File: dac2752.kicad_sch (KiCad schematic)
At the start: 39 parts, among them U30 LTC2752B, U301 OPA2197D, U305 DG419D, U31 OPA2189DGK, U32 OPA2388DGK

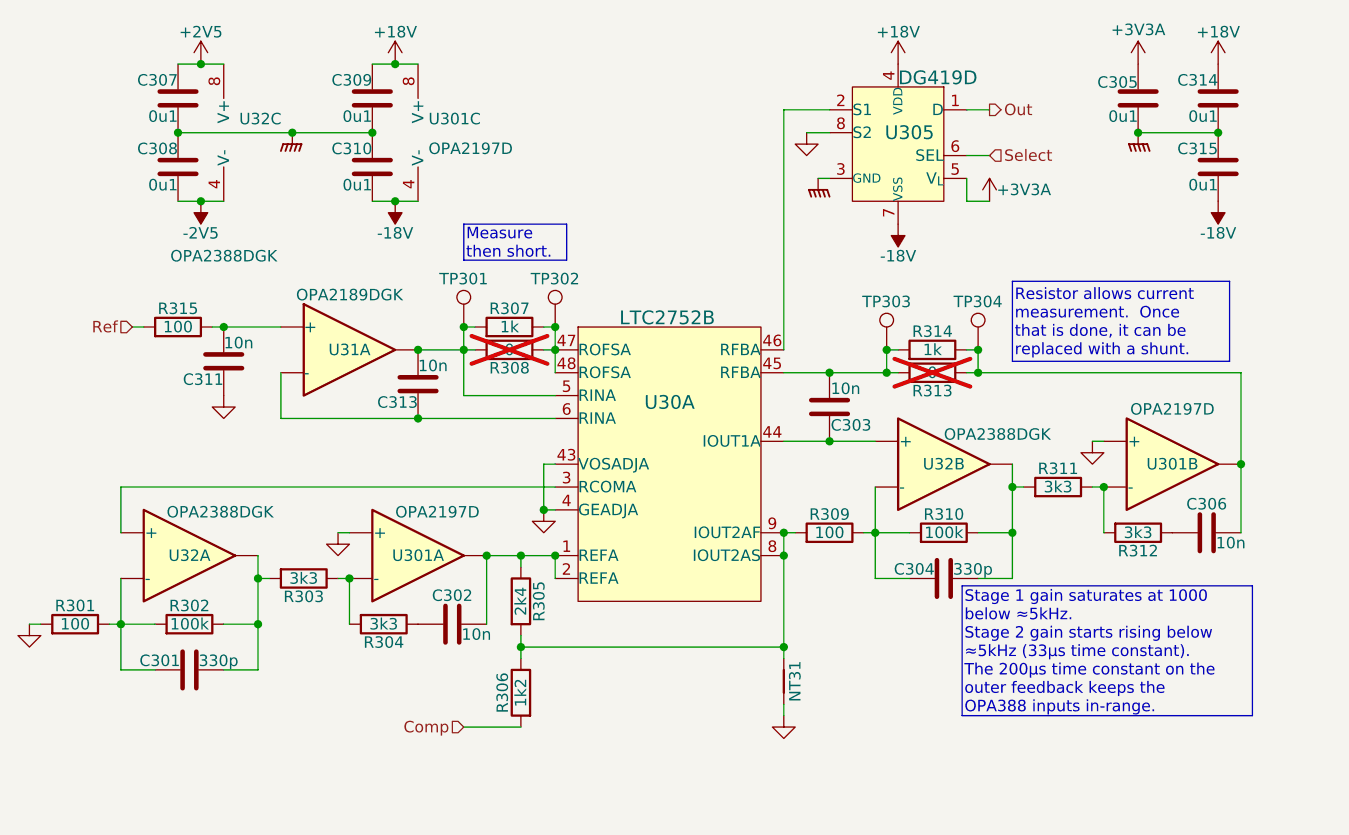
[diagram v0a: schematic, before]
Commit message: Whew.  DACs routed
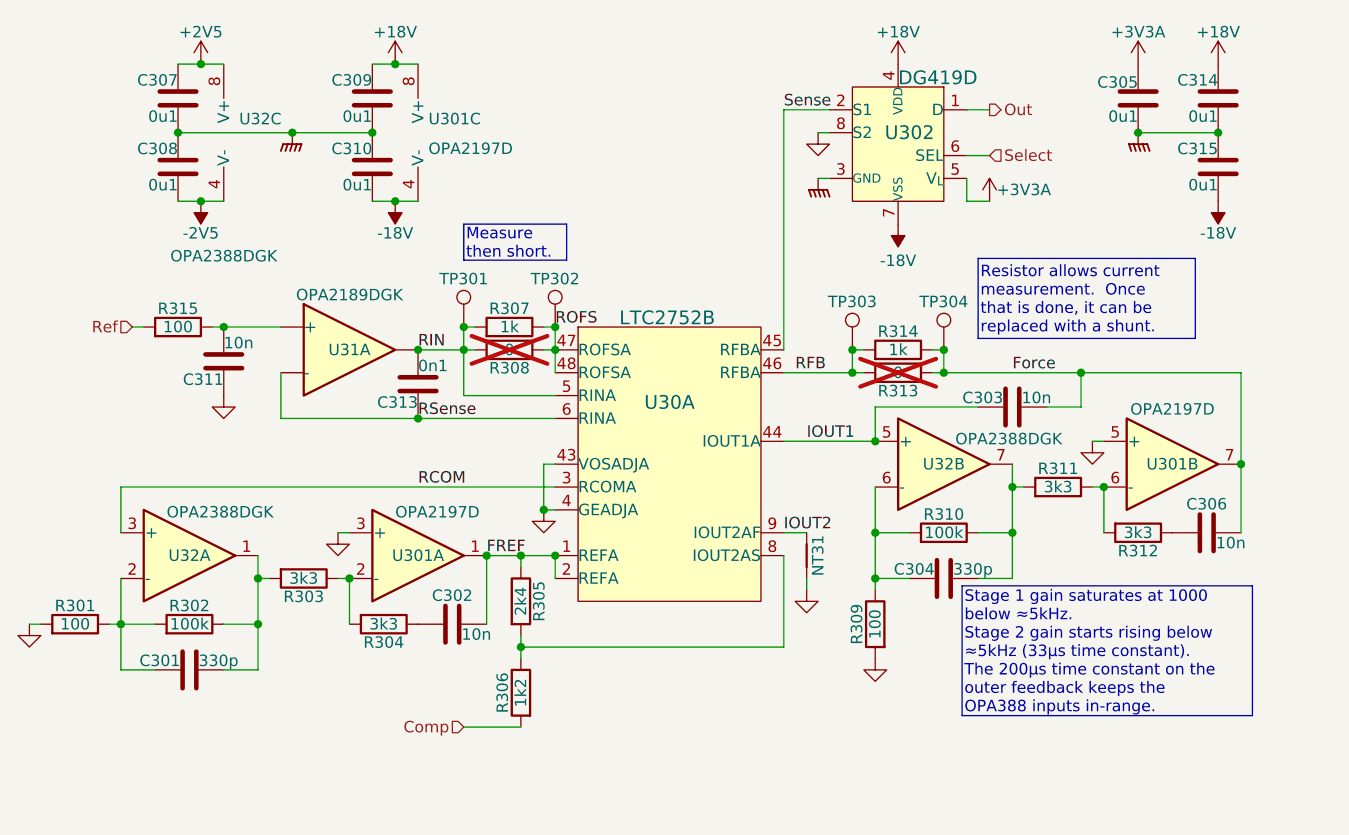
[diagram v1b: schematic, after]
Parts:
- C313: value 10n -> 0n1; footprint Capacitor_SMD:C_0603_1608Metric -> Capacitor_SMD:C_0402_1005Metric; LCSC C307500 -> C1546
- NT31: footprint NetTie:NetTie-2_SMD_Pad0.5mm -> Parts:NetTie-2_SMD_Pad0.5mm
- U30: footprint Package_QFP:LQFP-48_7x7mm_P0.5mm -> Parts:LQFP-48_7x7mm_P0.5mm
- U301: footprint Package_SO:SOIC-8_3.9x4.9mm_P1.27mm -> Parts:OPA2197; symbol Amplifier_Operational:OPA2197xD -> Parts:OPA2197D
- U31: footprint Package_SO:MSOP-8_3x3mm_P0.65mm -> Parts:OPA2189
- U32: footprint Package_SO:MSOP-8_3x3mm_P0.65mm -> Parts:OPA2388
- renumbered U305 to U302
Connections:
- net GND: now also R309.2
- net Force: now reaches C306.1, R313.1, R314.1, TP304.1, U301.7
- net Force: now also C303.2
- net IOUT1: now reaches U30.44 (IOUT1A), U32.5 (+)
- net IOUT1: now also C303.1; no longer C303.2
- net FREF: now reaches C302.1, R305.1, U30.1 (REFA), U30.2 (REFA), U301.1
- net RFB: now reaches R313.2, R314.2, TP303.1
- net RFB: now also U30.46 (RFBA); no longer C303.1, U30.45 (RFBA)
- net ROFS: now reaches R307.1, R308.1, TP302.1, U30.47 (ROFSA), U30.48 (ROFSA)
- net RIN: now reaches C313.1, R307.2, R308.2, TP301.1, U30.5 (RINA), U31.1
- net RCOM: now reaches U30.3 (RCOMA), U32.3 (+)
- net Sense: now reaches U302.2 (S1)
- net Sense: now also U30.45 (RFBA); no longer U30.46 (RFBA)
- net RSense: now reaches C313.2, U30.6 (RINA), U31.2 (-)
- net at R305.2, R306.1, U30.8 (IOUT2AS): no longer NT31.2, R309.2, U30.9 (IOUT2AF)
- new net IOUT2: NT31.2, U30.9 (IOUT2AF)
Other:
- moved on the sheet: C303, NT31, R309, R314, TP303, TP304

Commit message: Tweaks following spice simulation.
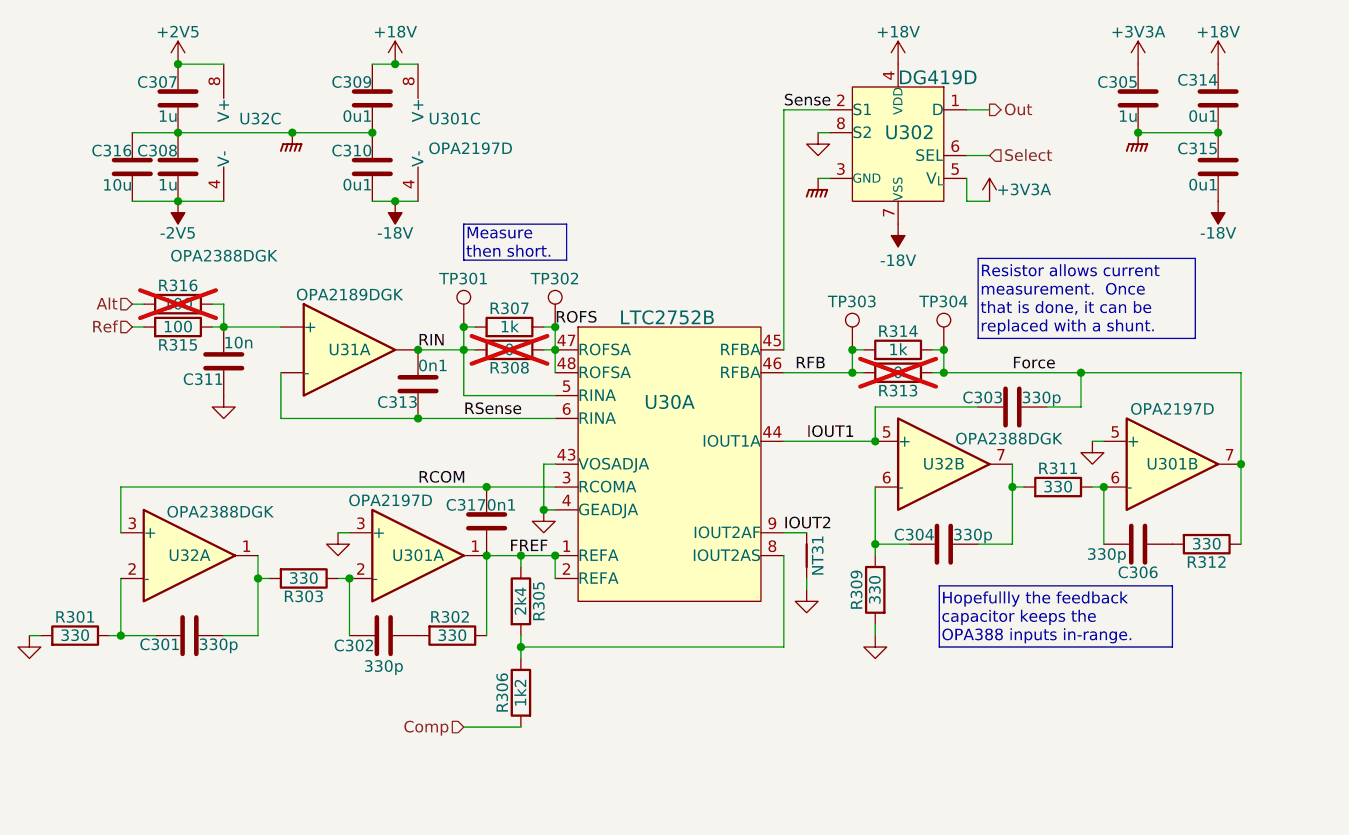
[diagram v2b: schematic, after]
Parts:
- removed R304: 3k3, Resistor_SMD:R_0603_1608Metric, symbol Device:R
- removed R310: 100k, Resistor_SMD:R_0603_1608Metric, symbol Device:R
- added C316: 10u, Capacitor_SMD:C_0603_1608Metric, symbol Device:C
- added C317: 0n1, Capacitor_SMD:C_0402_1005Metric, symbol Device:C
- added R316: 100, Resistor_SMD:R_0603_1608Metric, symbol Device:R
- C302, C303, C306: value 10n -> 330p; LCSC C307500 -> C1664
- C305, C307, C308: value 0u1 -> 1u; LCSC C307331 -> C52923
- R301, R309: value 100 -> 330; footprint Resistor_SMD:R_0603_1608Metric -> Resistor_SMD:R_0402_1005Metric; LCSC C23140 -> C25104
- R302: value 100k -> 330; footprint Resistor_SMD:R_0603_1608Metric -> Resistor_SMD:R_0402_1005Metric; LCSC C4216 -> C25104
- R303, R311, R312: value 3k3 -> 330; footprint Resistor_SMD:R_0603_1608Metric -> Resistor_SMD:R_0402_1005Metric; LCSC C22978 -> C25104
- R315: footprint Resistor_SMD:R_0402_1005Metric -> Resistor_SMD:R_0603_1608Metric
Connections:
- net -2V5: now also C316.2
- net FREF: now also R302.1, C317.2; no longer C302.1
- net Force: now also R312.1; no longer C306.1
- net GNDPWR: now also C316.1
- net RCOM: now also C317.1
- net at R311.1, U301.6 (-): now also C306.2; no longer R312.2
- net at R303.1, U301.2 (-): now also C302.2
- net at C301.1, R303.2, U32.1: no longer R302.1
- net at C301.2, R301.1, U32.2 (-): no longer R302.2
- net at C311.1, R315.1, U31.3 (+): now also R316.1
- new net: C302.1, R302.2
- new net: C306.1, R312.2
- new net Alt: R316.2
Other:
- moved on the sheet: C301, C302, C304, C306, R301, R309, R312

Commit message: About to delete scan...
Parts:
- R308, R313: Stock (none) -> 40
- R316: LCSC C25076 -> (none); Stock (none) -> 40
- TP301, TP302, TP303, TP304: Stock (none) -> -
- U301: Stock (none) -> 30
- U31: Stock (none) -> 15
- U32: Stock (none) -> 14

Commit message: Scan deleted.
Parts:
- R315: LCSC C25076 -> C22775
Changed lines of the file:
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@@
 			)
 		)
-		(property "Datasheet" "50V"
+		(property "Datasheet" "X7R, 50V"
 			(at 184.15 50.8 0)
 			(effects
@@
 			)
 		)
-		(property "Datasheet" "50V"
+		(property "Datasheet" "X7R, 50V"
 			(at 90.17 50.8 0)
 			(effects
@@
 			)
 		)
-		(property "LCSC" "C25076"
+		(property "LCSC" "C22775"
 			(at 68.58 76.2 90)
 			(effects
@@
 			)
 		)
-		(property "Datasheet" "50V"
+		(property "Datasheet" "X7R, 50V"
 			(at 90.17 58.42 0)
 			(effects
@@
 			)
 		)
-		(property "Datasheet" "50V"
+		(property "Datasheet" "X7R, 50V"
 			(at 184.15 58.42 0)
 			(effects

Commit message: Most blocks there....
About to restore scan.
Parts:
- removed C313: 0n1, Capacitor_SMD:C_0402_1005Metric, symbol Device:C
- removed C316: 10u, Capacitor_SMD:C_0603_1608Metric, symbol Device:C
- removed NT31: NetTie_2, Parts:NetTie-2_SMD_Pad0.5mm, symbol Parts:NetTie_2
- removed R305: 2k4, Resistor_SMD:R_0402_1005Metric, symbol Device:R
- removed R306: 1k2, Resistor_SMD:R_0402_1005Metric, symbol Device:R
- removed R307, R314: 1k, Resistor_SMD:R_0402_1005Metric, symbol Device:R
- removed R308, R313: 0, Resistor_SMD:R_0603_1608Metric, symbol Device:R
- removed TP301, TP302, TP303, TP304: TestPoint, Parts:TestPoint, symbol Connector:TestPoint
- added U34: OPA2388DGK, Parts:OPA2388, symbol Parts:OPA2388DGK
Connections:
- net RFB is gone; now on net Force: U30.46 (RFBA)
- net ROFS is gone; now on net RIN: U30.47 (ROFSA), U30.48 (ROFSA)
- net GND: now also R309.1, U34.5 (+); no longer R309.2
- net at C304.2, U32.6 (-): now also R309.2; no longer R309.1
- net at U30.8 (IOUT2AS): now also U34.6 (-)
- net IOUT2: no longer names the net of U30.9 (IOUT2AF)
- net IOUT2: now also U34.7
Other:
- moved on the sheet: C303, C304, C305, C306, C307, C308, C309, C310, C314, C315, R309, R311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

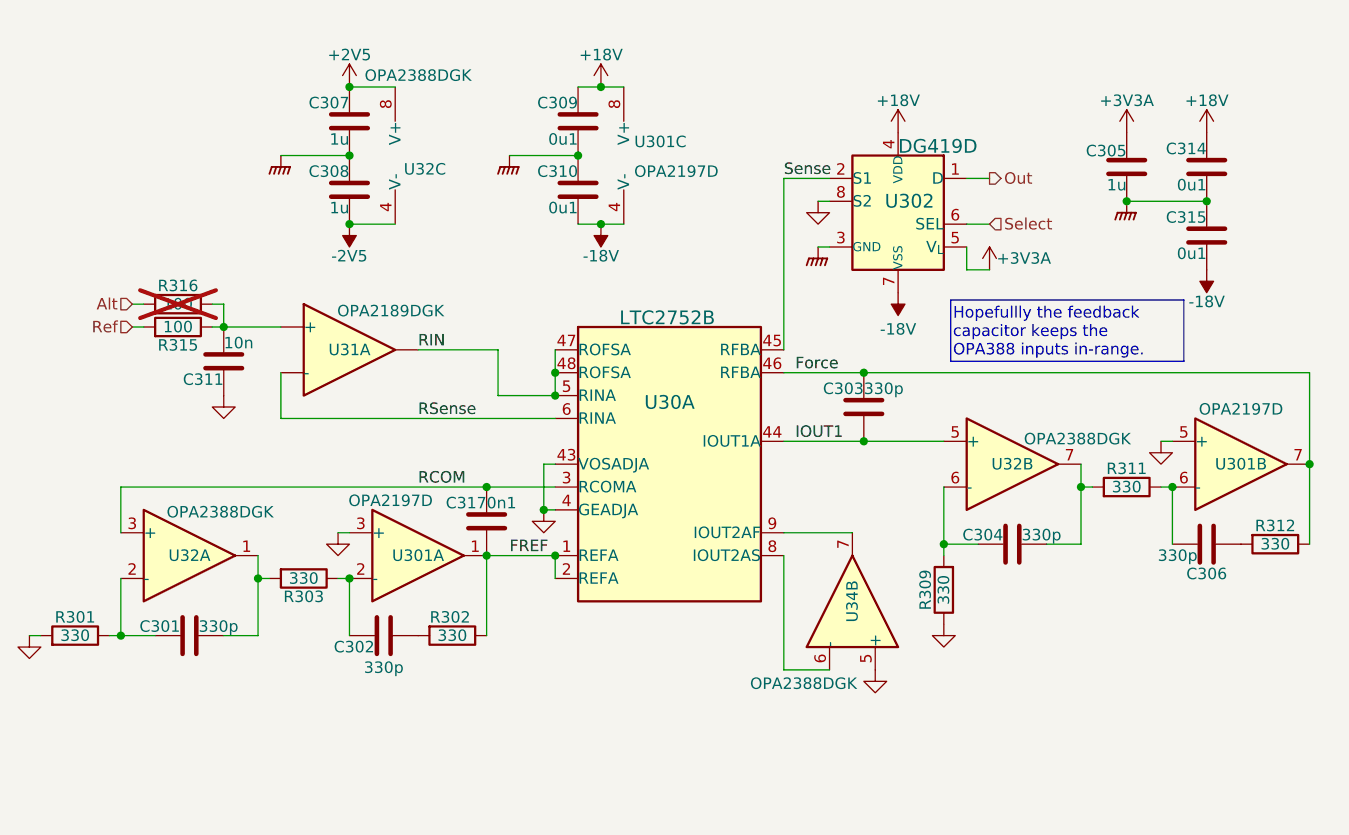
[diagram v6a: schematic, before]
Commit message: Put ref filtering into the schematic.
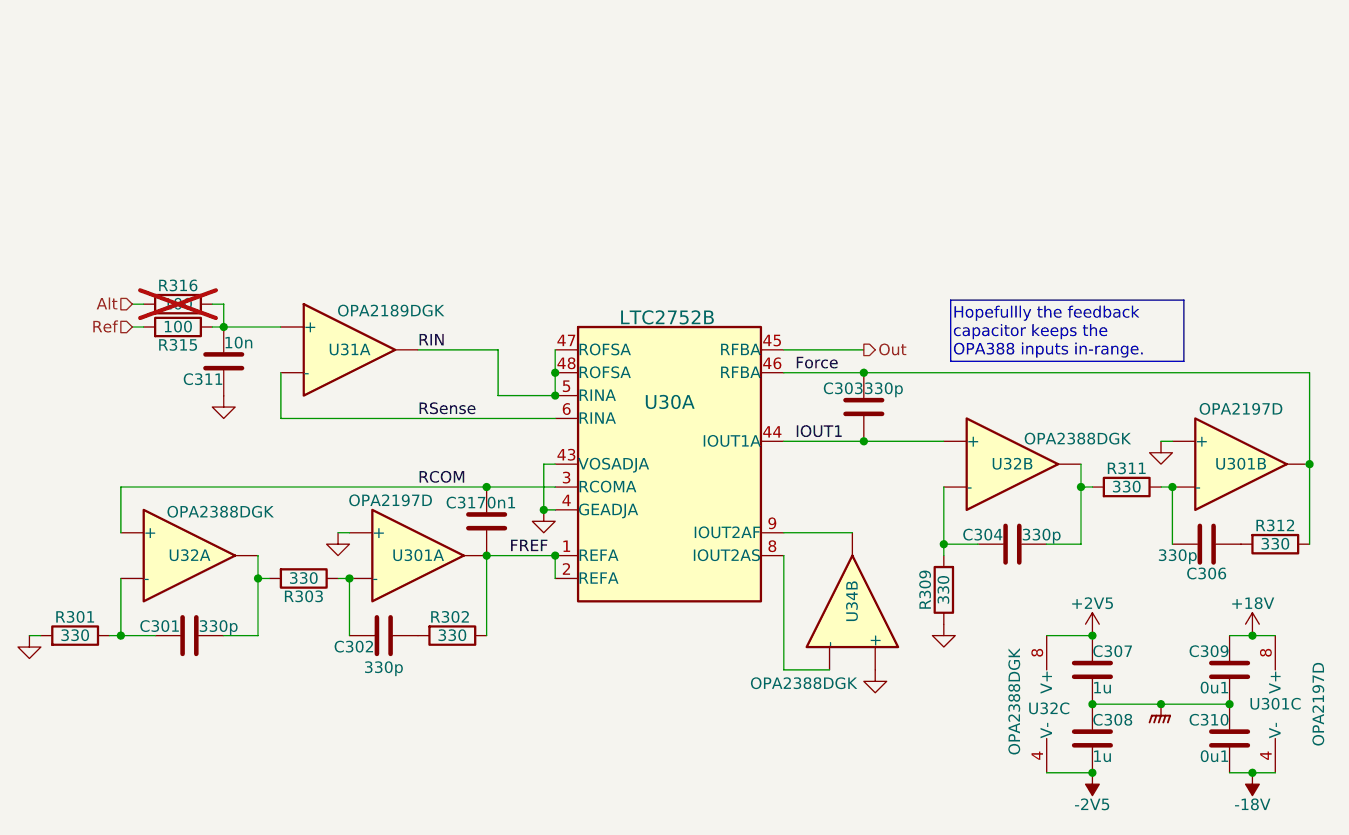
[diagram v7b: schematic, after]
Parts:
- removed C305: 1u, Capacitor_SMD:C_0402_1005Metric, symbol Device:C
- removed C314, C315: 0u1, Capacitor_SMD:C_0402_1005Metric, symbol Device:C
- removed U302: DG419D, Package_SO:SOIC-8_3.9x4.9mm_P1.27mm, symbol Parts:DG419
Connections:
- net Sense is gone; now on net Out: U30.45 (RFBA)
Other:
- moved on the sheet: C307, C308, C309, C310, U301C, U32C

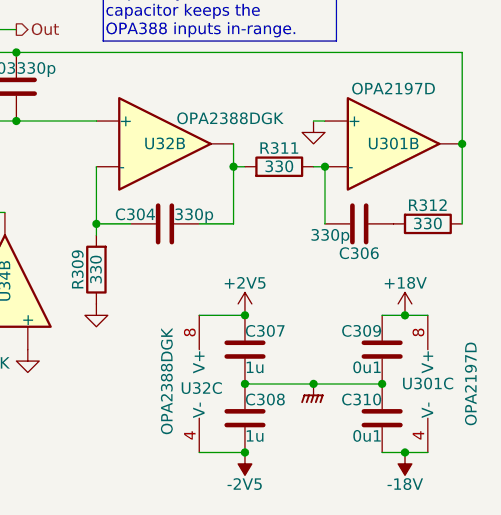
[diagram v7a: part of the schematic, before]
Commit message: Adjust voltage rails.
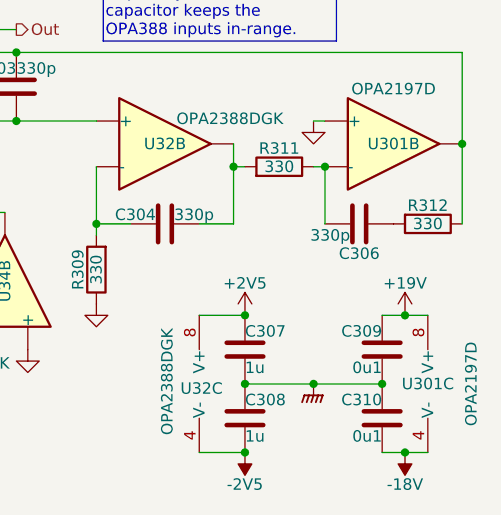
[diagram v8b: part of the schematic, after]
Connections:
- net +18V renamed +19V
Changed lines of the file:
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@@
 	)
 	(symbol
-		(lib_id "Parts:+18V")
+		(lib_id "Parts:+19V")
 		(at 187.96 110.49 0)
 		(unit 1)
@@
 		(on_board yes)
 		(dnp no)
-		(property "Reference" "#PWR0264"
+		(property "Reference" "#PWR264"
 			(at 187.96 114.3 0)
 			(effects
@@
 			)
 		)
-		(property "Value" "+18V"
+		(property "Value" "+19V"
 			(at 187.96 106.934 0)
 			(do_not_autoplace yes)
@@
 			)
 		)
-		(property "Description" "Power symbol creates a global label with name {dblquote}+18V{dblquote}"
+		(property "Description" "Power symbol creates a global label with name \"+19\""
 			(at 187.96 110.49 0)
 			(effects
@@
 			(project "lincal"
 				(path "/b054cef4-39e3-49d8-aff0-7ba5a206c187/361a423f-d05f-4f8b-bc28-600b62434109"
-					(reference "#PWR0165")
+					(reference "#PWR165")
 					(unit 1)
 				)
 				(path "/b054cef4-39e3-49d8-aff0-7ba5a206c187/460d889b-fb9b-4b3e-8128-6fba79ce7ab4"
-					(reference "#PWR0275")
+					(reference "#PWR275")
 					(unit 1)
 				)
 				(path "/b054cef4-39e3-49d8-aff0-7ba5a206c187/aeb3a378-4287-41b1-9e33-8dbd035c4d66"
-					(reference "#PWR0286")
+					(reference "#PWR286")
 					(unit 1)
 				)
 				(path "/b054cef4-39e3-49d8-aff0-7ba5a206c187/f2e682f2-52ca-4ed0-8a7d-aeb09fbc9914"
-					(reference "#PWR0264")
+					(reference "#PWR264")
 					(unit 1)
 				)
